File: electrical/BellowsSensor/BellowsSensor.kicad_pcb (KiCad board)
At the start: 2 copper layers, 30 x 20 mm, 5 parts, among them J1 I2C, U1 ELVH-001D-HRRJ-C-N2A4

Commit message: Use TITLE variable in silkscreen
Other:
- board text added: "${TITLE} Rev ${REVISION}"
- board text removed: "MIDI Concertina Bellows Sensor Rev ${REVISION}"
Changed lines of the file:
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@@
 	(paper "USLetter")
 	(title_block
-		(title "MIDI Concertina Bellows Sensor")
+		(title "MIDI Bellows Sensor")
 		(rev "1")
 		(comment 1 "https://ohwr.org/cern_ohl_s_v2.pdf")
@@
 		(layer "Edge.Cuts")
 	)
-	(gr_text "MIDI Concertina\nBellows Sensor\nRev ${REVISION}"
+	(gr_text "${TITLE}\nRev ${REVISION}"
 		(at 156 96 0)
 		(layer "B.SilkS")

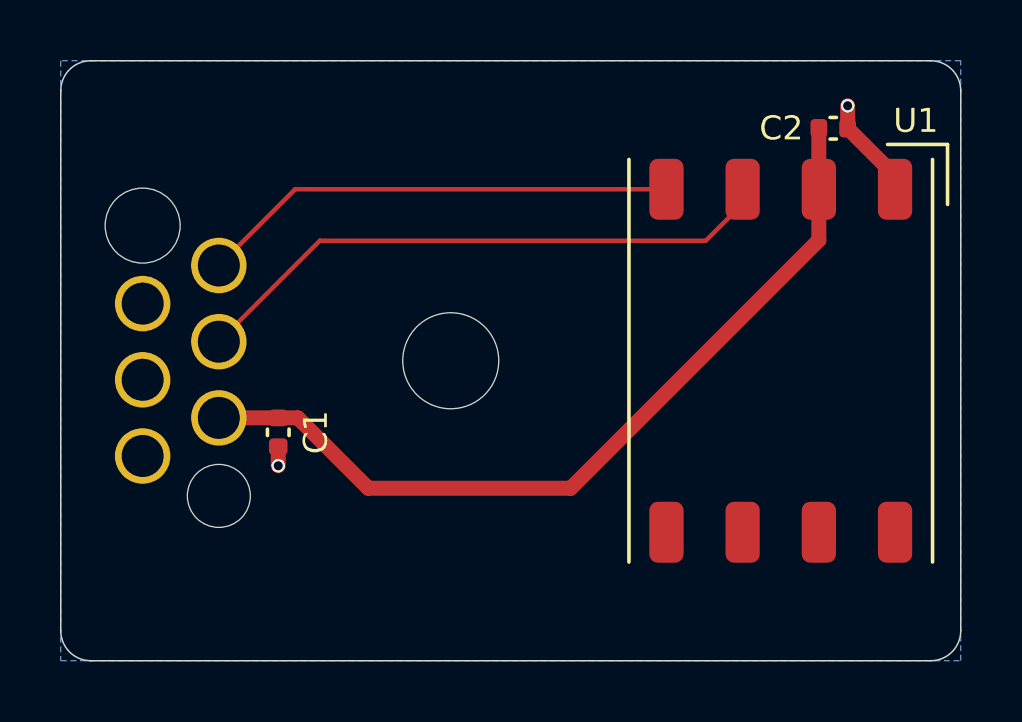
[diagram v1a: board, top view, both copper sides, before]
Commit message: Change i2c cable pinout to keep signals between grounds
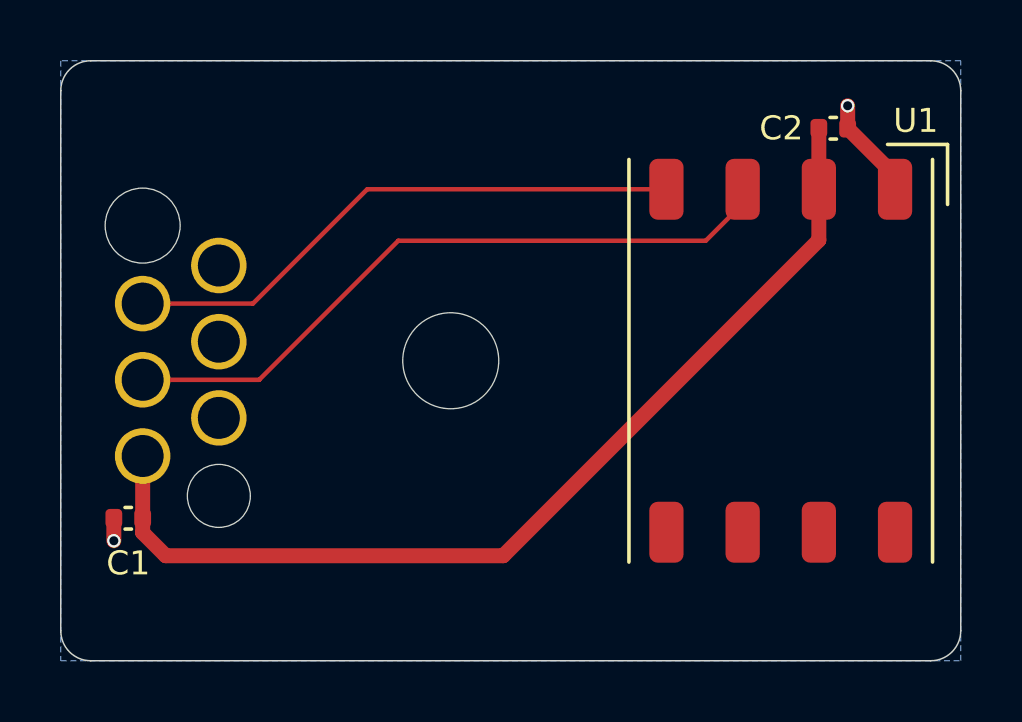
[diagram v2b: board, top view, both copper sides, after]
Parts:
- moved C1 5.76 mm to (130.2, 109.2), turned to 180 degrees
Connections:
- J1 pad 1: /I2C_SCL -> GND
- J1 pad 2: GND -> /I2C_SCL
- J1 pad 3: /I2C_SDA -> GND
- J1 pad 4: GND -> /I2C_SDA
- J1 pad 5: +3.3V -> GND
- J1 pad 6: GND -> +3.3V
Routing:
- net +3.3V: track 28.1 -> 33.5 mm
- net /I2C_SDA: track 19.8 -> 22.9 mm
- net /I2C_SCL: track 16.0 -> 19.0 mm
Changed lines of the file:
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@@
 	(footprint "Capacitor_SMD:C_0402_1005Metric"
 		(layer "F.Cu")
-		(at 135.25 106.385 -90)
+		(at 130.25 109.25 180)
 		(descr "Capacitor SMD 0402 (1005 Metric), square (rectangular) end terminal, IPC-7351 nominal, (Body size source: IPC-SM-782 page 76, https://www.pcb-3d.com/wordpress/wp-content/uploads/ipc-sm-782a_amendment_1_and_2.pdf), generated with kicad-footprint-generator")
 		(tags "capacitor")
 		(property "Reference" "C1"
-			(at 0 -1.25 90)
+			(at 0 -1.5 0)
 			(layer "F.SilkS")
 			(effects
@@
 		)
 		(property "Value" "100n"
-			(at 0 1.16 90)
+			(at 0 1.16 0)
 			(layer "F.Fab")
 			(hide yes)
@@
 		)
 		(property "Datasheet" "https://mm.digikey.com/Volume0/opasdata/d220001/medias/docus/609/CL05B104KO5NNNC.pdf"
-			(at 0 0 90)
+			(at 0 0 0)
 			(layer "F.Fab")
 			(hide yes)
@@
 		)
 		(property "Description" "16V 100nF X7R ±10% Multilayer Ceramic Capacitor, ROHS"
-			(at 0 0 90)
+			(at 0 0 0)
 			(layer "F.Fab")
 			(hide yes)
@@
 		)
 		(property "LCSC" "C1525"
-			(at 0 0 270)
+			(at 0 0 180)
 			(unlocked yes)
 			(layer "F.Fab")
@@
 		)
 		(property "Part" "Samsung CL05B104KO5NNNC"
-			(at 0 0 270)
+			(at 0 0 180)
 			(unlocked yes)
 			(layer "F.Fab")
@@
 		)
 		(fp_line
+			(start 0.91 0.46)
+			(end -0.91 0.46)
+			(stroke
+				(width 0.05)
+				(type solid)
+			)
+			(layer "F.CrtYd")
+		)
+		(fp_line
+			(start 0.91 -0.46)
+			(end 0.91 0.46)
+			(stroke
+				(width 0.05)
+				(type solid)
+			)
+			(layer "F.CrtYd")
+		)
+		(fp_line
 			(start -0.91 0.46)
 			(end -0.91 -0.46)
@@
 		)
 		(fp_line
-			(start 0.91 0.46)
-			(end -0.91 0.46)
-			(stroke
-				(width 0.05)
-				(type solid)
-			)
-			(layer "F.CrtYd")
-		)
-		(fp_line
 			(start -0.91 -0.46)
 			(end 0.91 -0.46)
@@
 		)
 		(fp_line
-			(start 0.91 -0.46)
-			(end 0.91 0.46)
-			(stroke
-				(width 0.05)
-				(type solid)
-			)
-			(layer "F.CrtYd")
+			(start 0.5 0.25)
+			(end -0.5 0.25)
+			(stroke
+				(width 0.1)
+				(type solid)
+			)
+			(layer "F.Fab")
+		)
+		(fp_line
+			(start 0.5 -0.25)
+			(end 0.5 0.25)
+			(stroke
+				(width 0.1)
+				(type solid)
+			)
+			(layer "F.Fab")
 		)
 		(fp_line
@@
 		)
 		(fp_line
-			(start 0.5 0.25)
-			(end -0.5 0.25)
-			(stroke
-				(width 0.1)
-				(type solid)
-			)
-			(layer "F.Fab")
-		)
-		(fp_line
 			(start -0.5 -0.25)
 			(end 0.5 -0.25)
@@
 			(layer "F.Fab")
 		)
-		(fp_line
-			(start 0.5 -0.25)
-			(end 0.5 0.25)
-			(stroke
-				(width 0.1)
-				(type solid)
-			)
-			(layer "F.Fab")
-		)
 		(fp_text user "${REFERENCE}"
-			(at 0 0 90)
+			(at 0 0 0)
 			(layer "F.Fab")
 			(effects
@@
 		)
 		(pad "1" smd roundrect
-			(at -0.48 0 270)
+			(at -0.48 0 180)
 			(size 0.56 0.62)
 			(layers "F.Cu" "F.Mask" "F.Paste")
@@
 		)
 		(pad "2" smd roundrect
-			(at 0.48 0 270)
+			(at 0.48 0 180)
 			(size 0.56 0.62)
 			(layers "F.Cu" "F.Mask" "F.Paste")
@@
 			(layers "*.Cu" "*.Mask")
 			(remove_unused_layers no)
-			(net 3 "/I2C_SCL")
+			(net 2 "GND")
 			(pinfunction "Pin_1")
 			(pintype "passive")
@@
 			(layers "*.Cu" "*.Mask")
 			(remove_unused_layers no)
-			(net 2 "GND")
+			(net 3 "/I2C_SCL")
 			(pinfunction "Pin_2")
 			(pintype "passive")
@@
 			(layers "*.Cu" "*.Mask")
 			(remove_unused_layers no)
-			(net 4 "/I2C_SDA")
+			(net 2 "GND")
 			(pinfunction "Pin_3")
 			(pintype "passive")
@@
 			(layers "*.Cu" "*.Mask")
 			(remove_unused_layers no)
-			(net 2 "GND")
+			(net 4 "/I2C_SDA")
 			(pinfunction "Pin_4")
 			(pintype "passive")
@@
 			(layers "*.Cu" "*.Mask")
 			(remove_unused_layers no)
-			(net 1 "+3.3V")
+			(net 2 "GND")
 			(pinfunction "Pin_5")
 			(pintype "passive")
@@
 			(layers "*.Cu" "*.Mask")
 			(remove_unused_layers no)
-			(net 2 "GND")
+			(net 1 "+3.3V")
 			(pinfunction "Pin_6")
 			(pintype "passive")
@@
 	)
 	(segment
-		(start 135.25 105.905)
-		(end 135.905 105.905)
-		(width 0.5)
-		(layer "F.Cu")
-		(net 1)
-	)
-	(segment
-		(start 145 108.25)
-		(end 153.27 99.98)
-		(width 0.5)
-		(layer "F.Cu")
-		(net 1)
-	)
-	(segment
-		(start 135.905 105.905)
-		(end 138.25 108.25)
-		(width 0.5)
-		(layer "F.Cu")
-		(net 1)
-	)
-	(segment
 		(start 153.27 96.25)
 		(end 153.27 98.284)
@@
 	)
 	(segment
-		(start 138.25 108.25)
-		(end 145 108.25)
+		(start 130.73 109.73)
+		(end 131.5 110.5)
 		(width 0.5)
 		(layer "F.Cu")
@@
 	)
 	(segment
-		(start 133.27 105.905)
-		(end 135.25 105.905)
+		(start 131.5 110.5)
+		(end 142.75 110.5)
+		(width 0.5)
+		(layer "F.Cu")
+		(net 1)
+	)
+	(segment
+		(start 142.75 110.5)
+		(end 153.27 99.98)
+		(width 0.5)
+		(layer "F.Cu")
+		(net 1)
+	)
+	(segment
+		(start 130.73 109.25)
+		(end 130.73 109.73)
 		(width 0.5)
 		(layer "F.Cu")
@@
 	)
 	(segment
-		(start 135.25 106.865)
-		(end 135.25 107.5)
+		(start 130.73 107.175)
+		(end 130.73 109.25)
 		(width 0.5)
 		(layer "F.Cu")
-		(net 2)
+		(net 1)
 	)
 	(segment
 		(start 154.23 95.5)
 		(end 154.23 96.25)
+		(width 0.5)
+		(layer "F.Cu")
+		(net 2)
+	)
+	(segment
+		(start 129.77 110)
+		(end 129.77 109.25)
 		(width 0.5)
 		(layer "F.Cu")
@@
 	)
 	(via
-		(at 135.25 107.5)
+		(at 129.77 110)
 		(size 0.45)
 		(drill 0.3)
@@
 	)
 	(segment
-		(start 135.811 98.284)
+		(start 138.216 98.284)
 		(end 148.19 98.284)
 		(width 0.15)
@@
 	)
 	(segment
-		(start 133.27 100.825)
-		(end 135.811 98.284)
+		(start 130.73 102.095)
+		(end 134.405 102.095)
 		(width 0.15)
 		(layer "F.Cu")
@@
 	)
 	(segment
-		(start 136.635 100)
-		(end 149.5 100)
+		(start 134.405 102.095)
+		(end 138.216 98.284)
+		(width 0.15)
+		(layer "F.Cu")
+		(net 3)
+	)
+	(segment
+		(start 150.73 98.77)
+		(end 150.73 98.284)
+		(width 0.15)
+		(layer "F.Cu")
+		(net 4)
+	)
+	(segment
+		(start 130.73 104.635)
+		(end 134.615 104.635)
+		(width 0.15)
+		(layer "F.Cu")
+		(net 4)
+	)
+	(segment
+		(start 134.615 104.635)
+		(end 139.25 100)
 		(width 0.15)
 		(layer "F.Cu")
@@
 	)
 	(segment
-		(start 150.73 98.77)
-		(end 150.73 98.284)
+		(start 139.25 100)
+		(end 149.5 100)
 		(width 0.15)
 		(layer "F.Cu")
-		(net 4)
-	)
-	(segment
-		(start 133.27 103.365)
-		(end 136.635 100)
-		(width 0.15)
-		(layer "F.Cu")
